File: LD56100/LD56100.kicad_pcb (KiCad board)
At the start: 2 copper layers, 12.7 x 10.4 mm, 3 parts, among them J1 Conn_01x04_Male, J2 Conn_01x04_Male, U1 LD56100

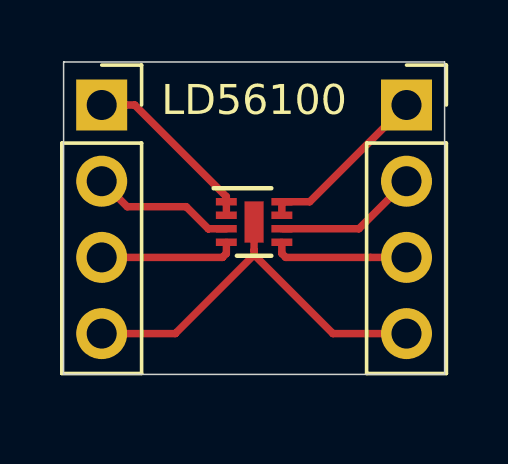
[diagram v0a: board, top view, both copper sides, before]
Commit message: build the gerbers for the LD56100, and build SOT-363
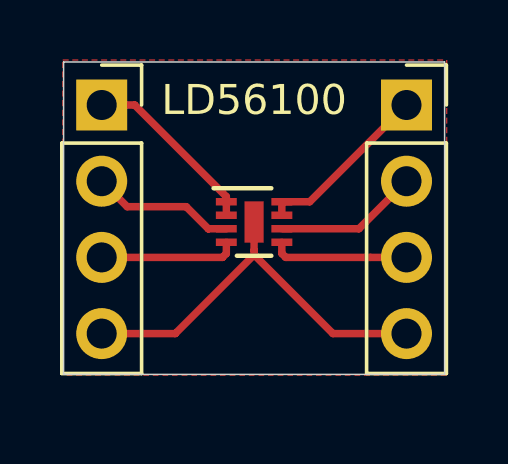
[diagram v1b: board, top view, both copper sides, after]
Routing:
- added copper zone on F.Cu, net PAD
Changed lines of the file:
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@@
     (last_trace_width 0.25)
     (trace_clearance 0.2)
-    (zone_clearance 0.508)
+    (zone_clearance 0.254)
     (zone_45_only no)
     (trace_min 0.2)
@@
       (drillshape 0)
       (scaleselection 1)
-      (outputdirectory ""))
+      (outputdirectory "../gerbers/LD56100-V1/"))
   )
   (net 0 "")
@@
   (segment (start 140.8 85) (end 143.855 88.055) (width 0.25) (layer F.Cu) (net 7))
   (segment (start 139.7 85) (end 140.8 85) (width 0.25) (layer F.Cu) (net 7))
+  (zone (net 1) (net_name PAD) (layer F.Cu) (hatch edge 0.508)
+    (connect_pads (clearance 0.254))
+    (min_thickness 0.254)
+    (fill yes (arc_segments 32) (thermal_gap 0.508) (thermal_bridge_width 0.508))
+    (polygon
+      (pts
+        (xy 151.2 94) (xy 138.4 94) (xy 138.4 83.5) (xy 151.2 83.5)
+      )
+    )
+  )
 )

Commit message: add the SOT-363 Part
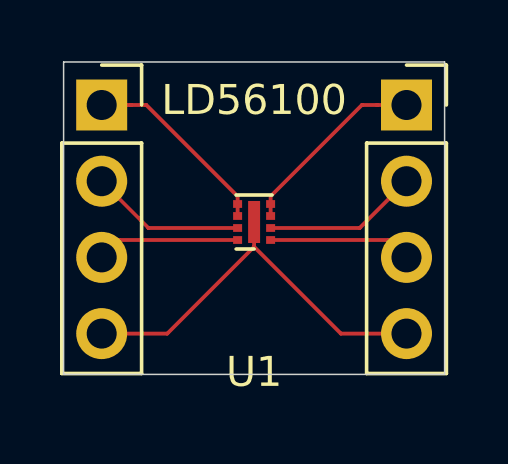
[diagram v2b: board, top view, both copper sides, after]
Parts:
- U1: footprint Package_DFN_QFN:DFN-8-1EP_2x2mm_P0.45mm_EP0.64x1.38mm -> Kevin-Lutzer-Kicad-Lbr:LD56100
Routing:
- net VIN: track 5.94 -> 6.45 mm
- removed copper zone on F.Cu, net PAD
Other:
- rule trace_min: 0.2 -> 0.05

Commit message: Update the LD56100 board to include pinout
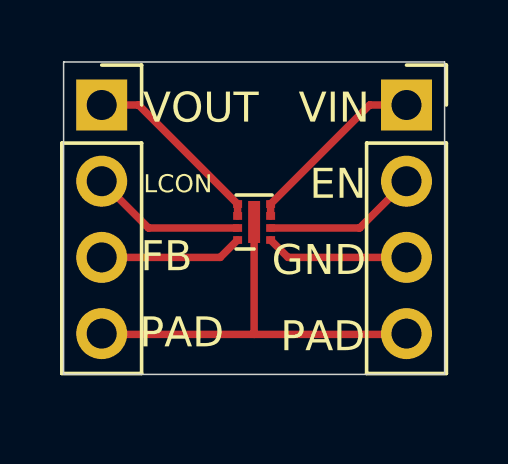
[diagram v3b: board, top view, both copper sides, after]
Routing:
- net PAD: track 13.4 -> 13.9 mm
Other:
- board text added: "EN"
- board text added: "FB"
- board text added: "GND"
- board text added: "LCON"
- board text added: "PAD"
- board text added: "REV1"
- board text added: "VIN"
- board text added: "VOUT"
